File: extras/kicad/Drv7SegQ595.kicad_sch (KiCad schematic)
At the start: 33 parts, among them IC1 74HC595, IC2 74HC595, J1 INTERFACE, J2 PWR_LED_JMP, Q1 MMBT3904, Q2 MMBT3904, Q3 MMBT3904, Q4 MMBT3904

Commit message: Rename all KiCAD files to correspond to this library's name.
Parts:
- DISPLAY1: footprint Drv7Seg2x595:display_7seg_4d_0.56in -> Drv7SegQ595:display_7seg_4d_0.56in; symbol Drv7Seg2x595:display_7seg_4d -> Drv7SegQ595:display_7seg_4d
- IC1, IC2: symbol Drv7Seg2x595:74HC595 -> Drv7SegQ595:74HC595
- J1: footprint Drv7Seg2x595:PinHeader_1x05_P2.54mm_Horizontal -> Connector_PinHeader_2.54mm:PinHeader_1x05_P2.54mm_Horizontal; symbol Drv7Seg2x595:pin_header_1-row_5-pin_horizontal -> Drv7SegQ595:pin_header_1-row_5-pin_horizontal
- J2: footprint Drv7Seg2x595:PinHeader_1x02_P2.54mm_Horizontal -> Drv7SegQ595:PinHeader_1x02_P2.54mm_Horizontal; symbol Drv7Seg2x595:pin_header_1-row_2-pin_horizontal -> Drv7SegQ595:pin_header_1-row_2-pin_horizontal
- Q1, Q2, Q3, Q4: footprint Drv7Seg2x595:SOT-23 -> Drv7SegQ595:SOT-23; symbol Drv7Seg2x595:MMBT3904 -> Drv7SegQ595:MMBT3904
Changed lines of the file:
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@@
 	(title_block
 		(date "15.12.2025")
-		(comment 1 "Documentation: github.com/ErlingSigurdson/Drv7Seg2x595")
+		(comment 1 "Documentation: github.com/ErlingSigurdson/Drv7SegQ595")
 		(comment 2 "Licensed under CERN-OHL-P v2")
 		(comment 3 "Copyright (c) 2025 Dmitriy Efimov aka Erling Sigurdson")
@@
 	)
 	(symbol
-		(lib_id "Drv7Seg2x595:74HC595")
+		(lib_id "Drv7SegQ595:74HC595")
 		(at 158.75 69.85 0)
 		(unit 1)
@@
 	)
 	(symbol
-		(lib_id "Drv7Seg2x595:MMBT3904")
+		(lib_id "Drv7SegQ595:MMBT3904")
 		(at 133.35 93.98 0)
 		(mirror y)
@@
 			)
 		)
-		(property "Footprint" "Drv7Seg2x595:SOT-23"
+		(property "Footprint" "Drv7SegQ595:SOT-23"
 			(at 128.27 95.885 0)
 			(effects
@@
 	)
 	(symbol
-		(lib_name "MountingHole_3")
 		(lib_id "Mechanical:MountingHole")
 		(at 234.95 102.87 0)
@@
 	)
 	(symbol
-		(lib_id "Drv7Seg2x595:display_7seg_4d")
+		(lib_id "Drv7SegQ595:display_7seg_4d")
 		(at 113.03 69.85 0)
 		(unit 1)
@@
 			)
 		)
-		(property "Footprint" "Drv7Seg2x595:display_7seg_4d_0.56in"
+		(property "Footprint" "Drv7SegQ595:display_7seg_4d_0.56in"
 			(at 112.522 96.52 0)
 			(effects
@@
 	)
 	(symbol
-		(lib_id "Drv7Seg2x595:MMBT3904")
+		(lib_id "Drv7SegQ595:MMBT3904")
 		(at 110.49 111.76 0)
 		(mirror y)
@@
 			)
 		)
-		(property "Footprint" "Drv7Seg2x595:SOT-23"
+		(property "Footprint" "Drv7SegQ595:SOT-23"
 			(at 105.41 113.665 0)
 			(effects
@@
 	)
 	(symbol
-		(lib_id "Drv7Seg2x595:MMBT3904")
+		(lib_id "Drv7SegQ595:MMBT3904")
 		(at 99.06 120.65 0)
 		(mirror y)
@@
 			)
 		)
-		(property "Footprint" "Drv7Seg2x595:SOT-23"
+		(property "Footprint" "Drv7SegQ595:SOT-23"
 			(at 93.98 122.555 0)
 			(effects
@@
 	)
 	(symbol
-		(lib_id "Drv7Seg2x595:pin_header_1-row_5-pin_horizontal")
+		(lib_id "Drv7SegQ595:pin_header_1-row_5-pin_horizontal")
 		(at 196.85 67.31 0)
 		(mirror y)
@@
 			)
 		)
-		(property "Footprint" "Drv7Seg2x595:PinHeader_1x05_P2.54mm_Horizontal"
+		(property "Footprint" "Connector_PinHeader_2.54mm:PinHeader_1x05_P2.54mm_Horizontal"
 			(at 196.342 80.772 0)
 			(effects
@@
 	)
 	(symbol
-		(lib_id "Drv7Seg2x595:74HC595")
+		(lib_id "Drv7SegQ595:74HC595")
 		(at 158.75 106.68 0)
 		(unit 1)
@@
 	)
 	(symbol
-		(lib_id "Drv7Seg2x595:MMBT3904")
+		(lib_id "Drv7SegQ595:MMBT3904")
 		(at 121.92 102.87 0)
 		(mirror y)
@@
 			)
 		)
-		(property "Footprint" "Drv7Seg2x595:SOT-23"
+		(property "Footprint" "Drv7SegQ595:SOT-23"
 			(at 116.84 104.775 0)
 			(effects
@@
 	)
 	(symbol
-		(lib_id "Drv7Seg2x595:pin_header_1-row_2-pin_horizontal")
+		(lib_id "Drv7SegQ595:pin_header_1-row_2-pin_horizontal")
 		(at 196.85 115.57 0)
 		(mirror y)
@@
 		(fields_autoplaced yes)
 		(property "Reference" "J2"
-			(at 196.215 102.87 0)
+			(at 198.12 106.6799 0)
 			(effects
 				(font
 					(size 1.27 1.27)
 				)
+				(justify right)
 			)
 		)
@@
 			)
 		)
-		(property "Footprint" "Drv7Seg2x595:PinHeader_1x02_P2.54mm_Horizontal"
+		(property "Footprint" "Drv7SegQ595:PinHeader_1x02_P2.54mm_Horizontal"
 			(at 195.072 117.094 0)
 			(effects
@@
 	)
 	(symbol
-		(lib_name "MountingHole_2")
 		(lib_id "Mechanical:MountingHole")
 		(at 234.95 90.17 0)
@@
 	)
 	(symbol
-		(lib_name "MountingHole_1")
 		(lib_id "Mechanical:MountingHole")
 		(at 234.95 109.22 0)

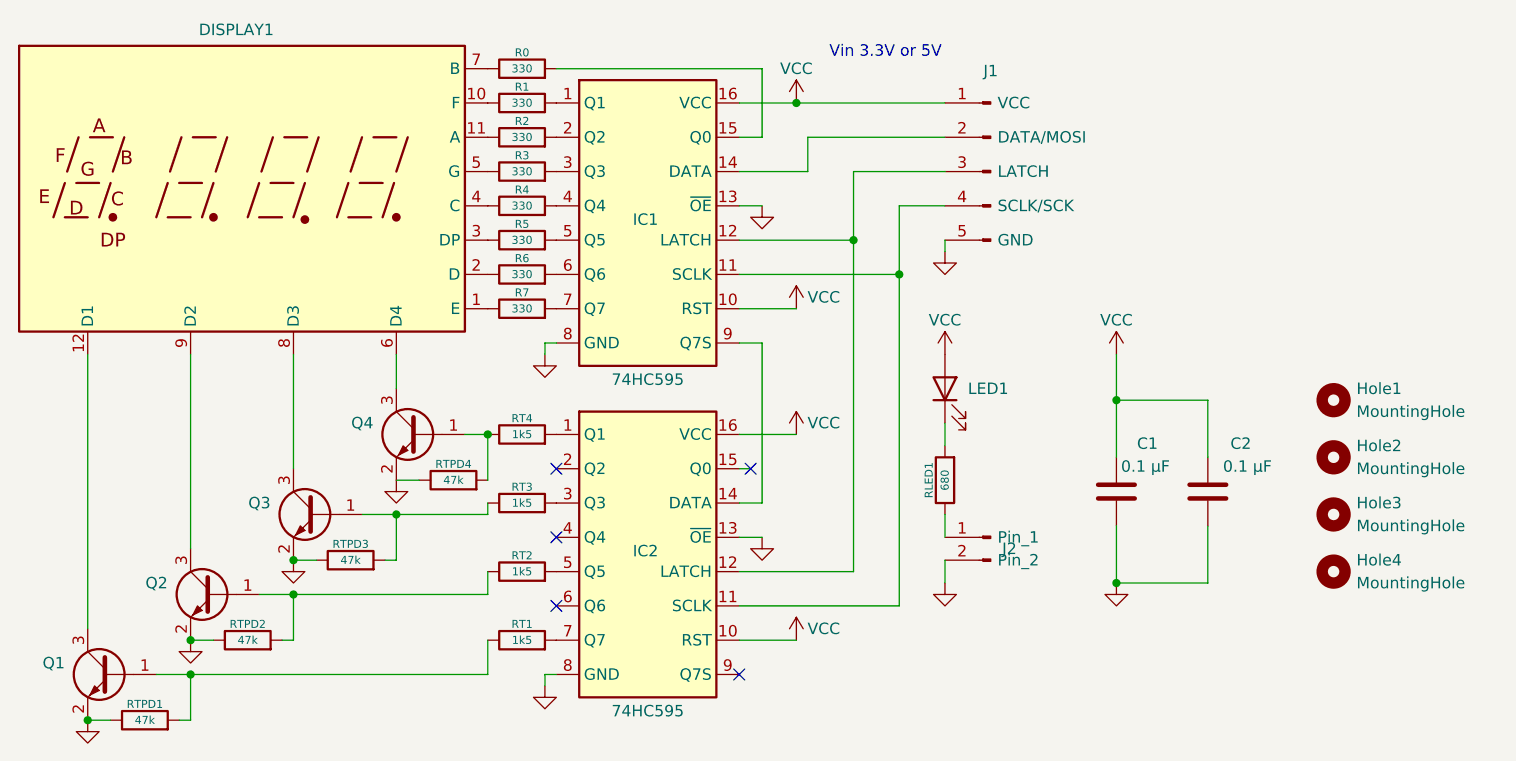
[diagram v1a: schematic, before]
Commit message: Update KiCAD files contents (mostly schematic) to match this library.
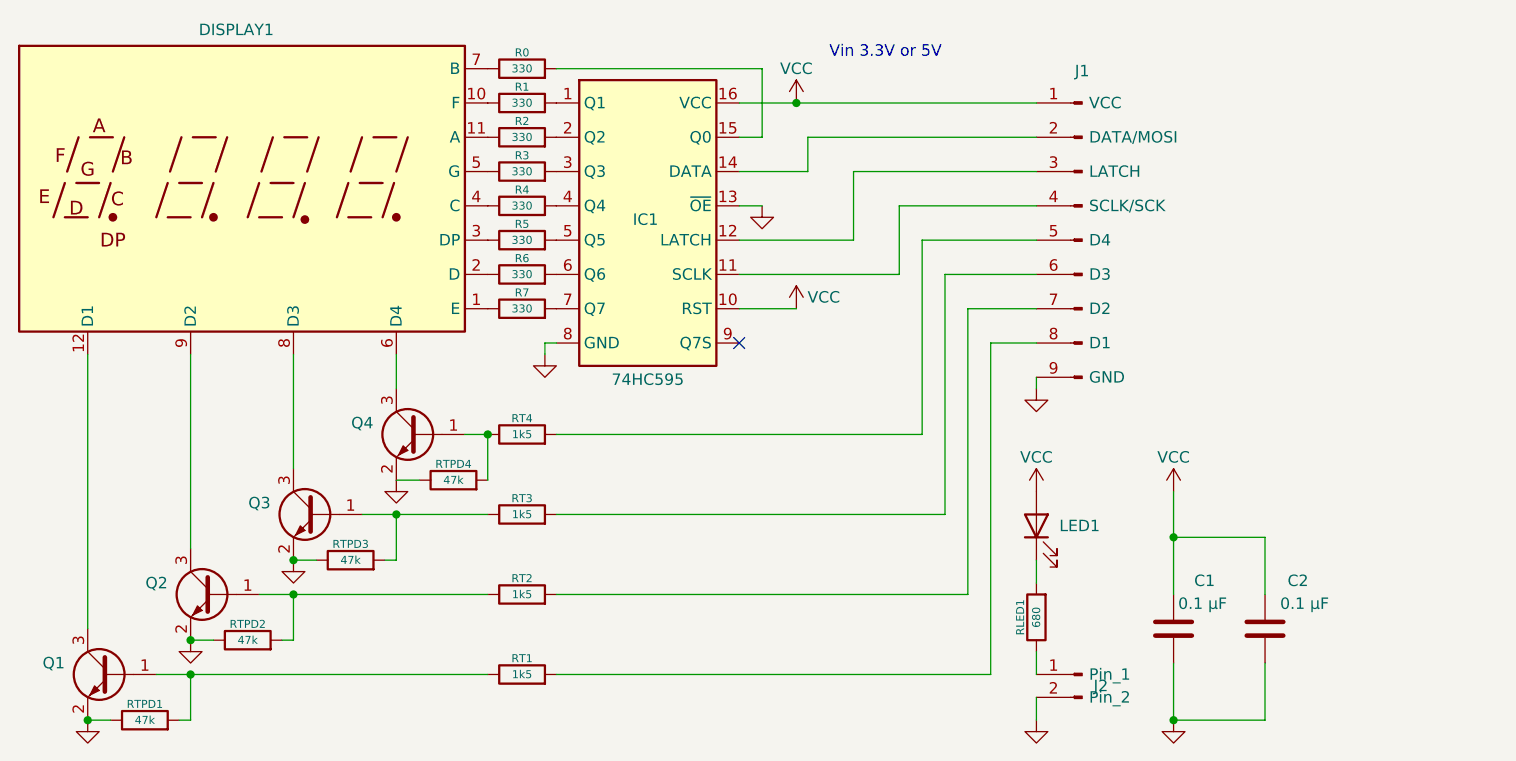
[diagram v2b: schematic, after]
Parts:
- removed Hole1, Hole2, Hole3, Hole4: MountingHole, MountingHole:MountingHole_3mm, symbol Mechanical:MountingHole
- removed IC2: 74HC595, Package_DIP:DIP-16_W7.62mm, symbol Drv7SegQ595:74HC595
- J1: symbol Drv7SegQ595:pin_header_1-row_5-pin_horizontal -> Drv7SegQ595:pin_header_1-row_9-pin_horizontal_abstract
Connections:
- net GND: now also J1.9 (GND); no longer J1.5 (GND)
- net at RT4.2: now also J1.5 (D4)
- net at RT1.2: now also J1.8 (D1)
- net at RT3.2: now also J1.6 (D3)
- net at RT2.2: now also J1.7 (D2)
- no-connect marks 5 -> 1
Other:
- moved on the sheet: C1, C2, J2, RLED1, RT1, RT2, RT3
